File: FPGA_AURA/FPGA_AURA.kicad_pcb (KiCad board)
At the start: 10 copper layers, 50 x 50 mm, 172 parts, among them J700 SS5-40-3.50-X-D-K-XX, J701 SS5-20-3.50-X-D-K-XX, U1 XC7A35T-2FTG256C, U100 ADP5014, U2 W25Q256JVEIQ, U4 TPS51200DRCR, U500 MT41K128M16JT-125_IT_K, Y500 ASEM1-100.000MHZ-LC-T

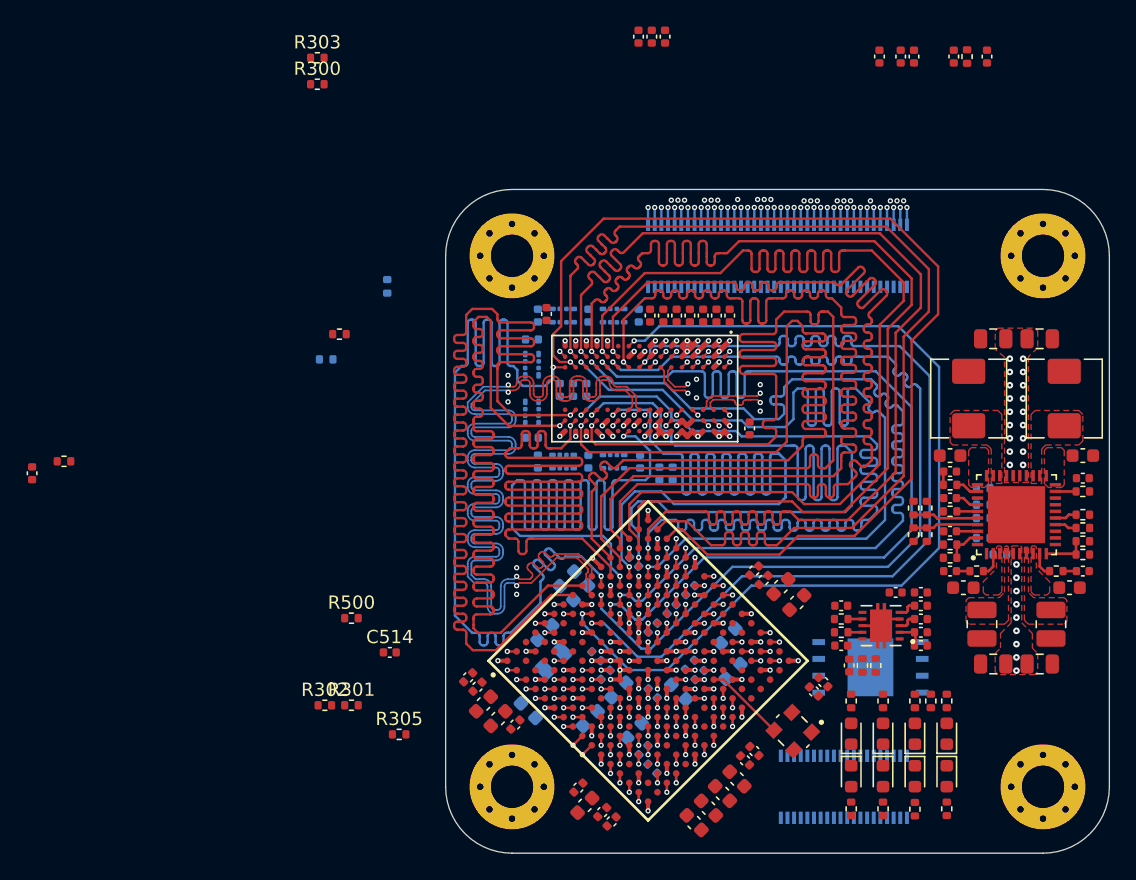
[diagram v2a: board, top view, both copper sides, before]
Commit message: All connector pins broken out. Next is QSPI flash, followed by power.
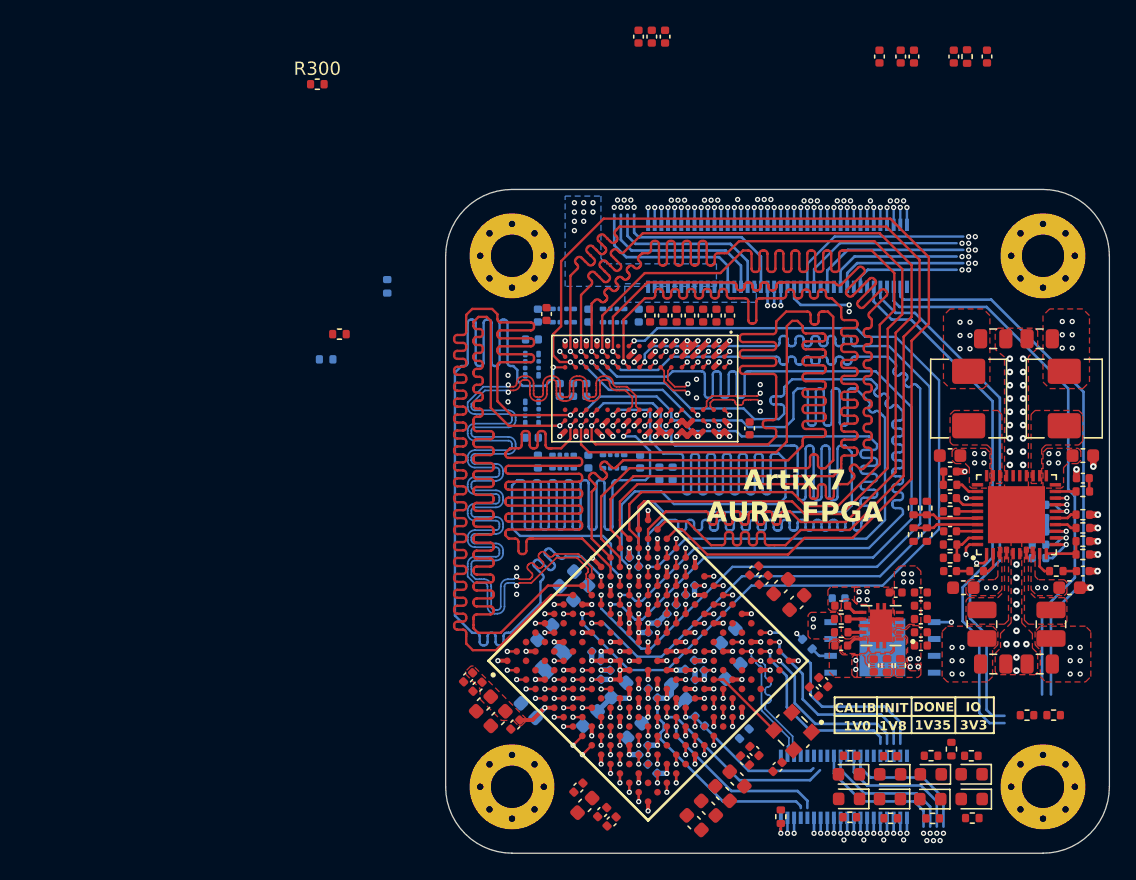
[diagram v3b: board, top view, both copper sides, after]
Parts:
- removed D1: LED, LED_SMD:LED_0603_1608Metric
- added D501: LED, LED_SMD:LED_0603_1608Metric, F.Cu at (139.6, 94.1)
- C300, R303, R304, R305: moved to B.Cu
- moved C300 61.5 mm to (129.6, 80.8), turned to 0 degrees
- moved R303 57.7 mm to (119.1, 90.1), turned to -45 degrees
- moved R304 57.7 mm to (127.2, 84.2), turned to -45 degrees
- moved R301 52.9 mm to (145.8, 89.6)
- moved R302 52.9 mm to (143.8, 89.6)
- moved R500 35.6 mm to (125.2, 97.2), turned to -90 degrees
- moved C514 30.5 mm to (125.0, 93.5), turned to -135 degrees
- moved R305 26.0 mm to (122.5, 91.0), turned to 45 degrees
- moved R502 4.53 mm to (139.6, 92.7), turned to 0 degrees
- moved R102 4.38 mm to (144.7, 73.8)
- moved R100 4.32 mm to (144.7, 74.8)
- moved R101 4.32 mm to (144.7, 75.8)
- moved R308 4.30 mm to (136.6, 92.7), turned to 0 degrees
- moved R103 4.23 mm to (144.7, 76.8)
- moved R306 4.19 mm to (133.5, 92.7), turned to 0 degrees
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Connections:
- J701 pad 03: TMS -> FPGA_REFCLK_P
- J701 pad 05: TCK -> FPGA_REFCLK_N
- J701 pad 08: FPGA_REFCLK_P -> TMS
- J701 pad 10: FPGA_REFCLK_N -> TCK
- U1 pad A2: ETH_1_TX_EN -> ETH_1_TXD_3
- U1 pad B1: ETH_1_TXD_1 -> ETH_1_TXD_2
- U1 pad C1: ETH_1_TXD_0 -> ETH_1_TXD_1
- U1 pad D1: ETH_1_TXD_3 -> ETH_1_TXD_0
- U1 pad E1: ETH_1_RXD_0 -> ETH_1_TX_EN
- U1 pad E2: ETH_1_TXD_2 -> ETH_1_RX_ER
- U1 pad F2: ETH_1_COL -> ETH_1_RXD_1
- U1 pad F3: ETH_1_CRS -> ETH_1_RXD_0
- U1 pad G1: ETH_1_RX_ER -> ETH_1_RXD_3
- U1 pad G2: ETH_1_RXD_3 -> ETH_1_RXD_2
- U1 pad G4: ETH_1_RXD_2 -> ETH_1_COL
- U1 pad G5: ETH_1_RXD_1 -> ETH_1_RX_DV
- U1 pad H1: ETH_0_RXD_1 -> ETH_0_TXD_3
- U1 pad H2: ETH_0_RXD_0 -> ETH_0_TXD_2
- U1 pad H3: ETH_0_RXD_3 -> ETH_0_TXD_1
- U1 pad H5: ETH_1_RX_DV -> ETH_1_CRS
- U1 pad J1: ETH_0_RX_DV -> ETH_0_TXD_0
- U1 pad J3: ETH_0_RXD_2 -> ETH_0_RX_DV
- U1 pad J4: ETH_0_COL -> ETH_0_RXD_0
- U1 pad J5: ETH_0_CRS -> ETH_0_RX_ER
- U1 pad K1: ETH_0_RX_ER -> ETH_0_TX_EN
- U1 pad K2: ETH_0_TXD_3 -> ETH_0_RXD_3
- U1 pad K3: ETH_0_TXD_2 -> ETH_0_CRS
- U1 pad K5: ETH_0_TX_EN -> ETH_0_COL
- U1 pad L2: ETH_0_TXD_1 -> ETH_0_RXD_2
- U1 pad L3: ETH_0_TXD_0 -> ETH_0_RXD_1
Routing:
- net MDIO: track 0.71 -> 42.0 mm, vias 1 -> 2
- net MDC: track 0.71 -> 41.9 mm, vias 1 -> 2
- net PHY_0_RST: track 0.71 -> 41.0 mm, vias 1 -> 2
- net PHY_1_RST: track 0.71 -> 40.1 mm, vias 1 -> 2
- net GND: track 66.5 -> 87.9 mm, vias 124 -> 174
- net ETH_1_TXD_2: track 69.8 -> 90.2 mm
- net ETH_1_TXD_3: track 73.0 -> 93.2 mm
- net ETH_0_TXD_1: track 65.1 -> 81.7 mm
- net SPI_SD_CS_0: track 0.71 -> 16.3 mm
- net TCK: track 0.71 -> 16.2 mm
- net ETH_0_TXD_3: track 67.6 -> 82.6 mm
- net ETH_0_TXD_2: track 67.3 -> 82.2 mm
- net SDA_1V8: track 0.71 -> 15.0 mm
- net SPI_SD_MOSI: track 0.71 -> 14.7 mm
- net SPI_1V8_CS_0: track 0.71 -> 14.6 mm
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- added copper zone on F.Cu, net +1V0
- added copper zone on F.Cu, net +1V35
- added copper zone on F.Cu, net +1V8
- added copper zone on F.Cu, net +3V3
- added copper zone on B.Cu, net +5V
- added copper zone on F.Cu, net +VTT
- added copper zone on F.Cu, net /100_Power_Regulation/ADP_SW1
- added copper zone on F.Cu, net /100_Power_Regulation/ADP_SW2
- added copper zone on F.Cu, net /100_Power_Regulation/ADP_SW3
- added copper zone on F.Cu, net /100_Power_Regulation/ADP_SW4
- added copper zone on F.Cu, net /100_Power_Regulation/TPS_REFIN
- added copper zone on B.Cu, net GND
- removed copper zone on F.Cu, net (none)
- removed copper zone on In3.Cu, net GND
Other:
- board text added: "1V0"
- board text added: "1V35"
- board text added: "1V8"
- board text added: "3V3"
- board text added: "Artix 7 AURA FPGA"
- board text added: "CALIB"
- board text added: "DONE"
- board text added: "INIT"
- board text added: "IO"

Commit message: Updated and validated Vivado MII pin assignments.
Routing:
- net SCL_3V3: track 1.87 -> 20.1 mm
- net UART_3V3_1_RX: track 1.87 -> 20.0 mm
- net UART_3V3_1_TX: track 1.87 -> 19.9 mm
- net SDA_3V3: track 1.87 -> 19.8 mm
- net UART_3V3_0_RX: track 1.87 -> 19.1 mm
- net /300_FPGA_Config/QSPI_IO0: track 0.71 -> 10.9 mm
- net /300_FPGA_Config/QSPI_IO1: track 0.71 -> 9.42 mm
- net ETH_0_TXD_3: track 82.6 -> 88.3 mm
- net ETH_0_TXD_2: track 82.2 -> 87.8 mm
- net ETH_0_TXD_1: track 81.7 -> 87.3 mm
- net ETH_0_TXD_0: track 77.3 -> 82.8 mm
- net GND: track 87.9 -> 93.2 mm
- net /300_FPGA_Config/QSPI_IO2: track 0.00 -> 5.15 mm
- net /300_FPGA_Config/QSPI_IO3: track 0.00 -> 2.32 mm, vias 0 -> 1
- net PHY_1_RST: track 40.1 -> 40.7 mm
